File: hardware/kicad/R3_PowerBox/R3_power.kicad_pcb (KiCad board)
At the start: 2 copper layers, 160 x 80 mm, 0 parts

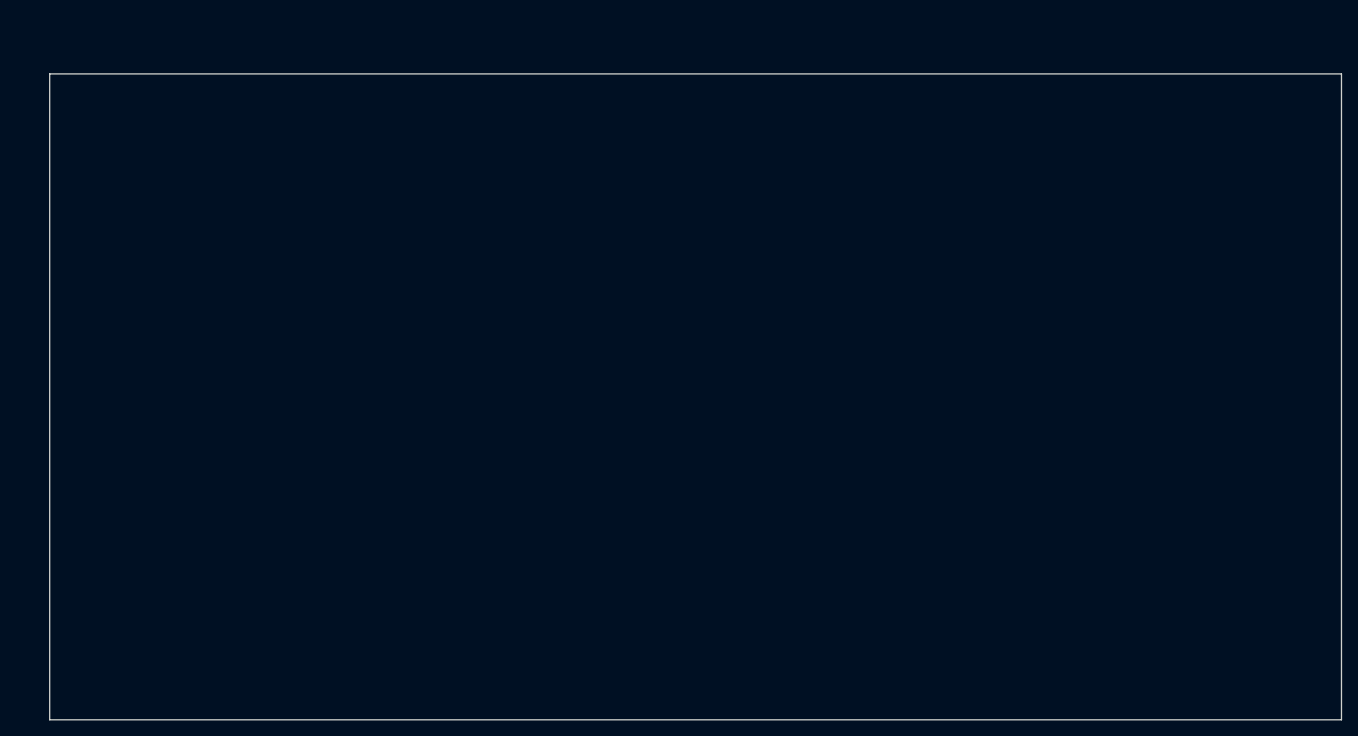
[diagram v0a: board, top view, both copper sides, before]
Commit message: Finalize R3 PowerBox pre-routing placement
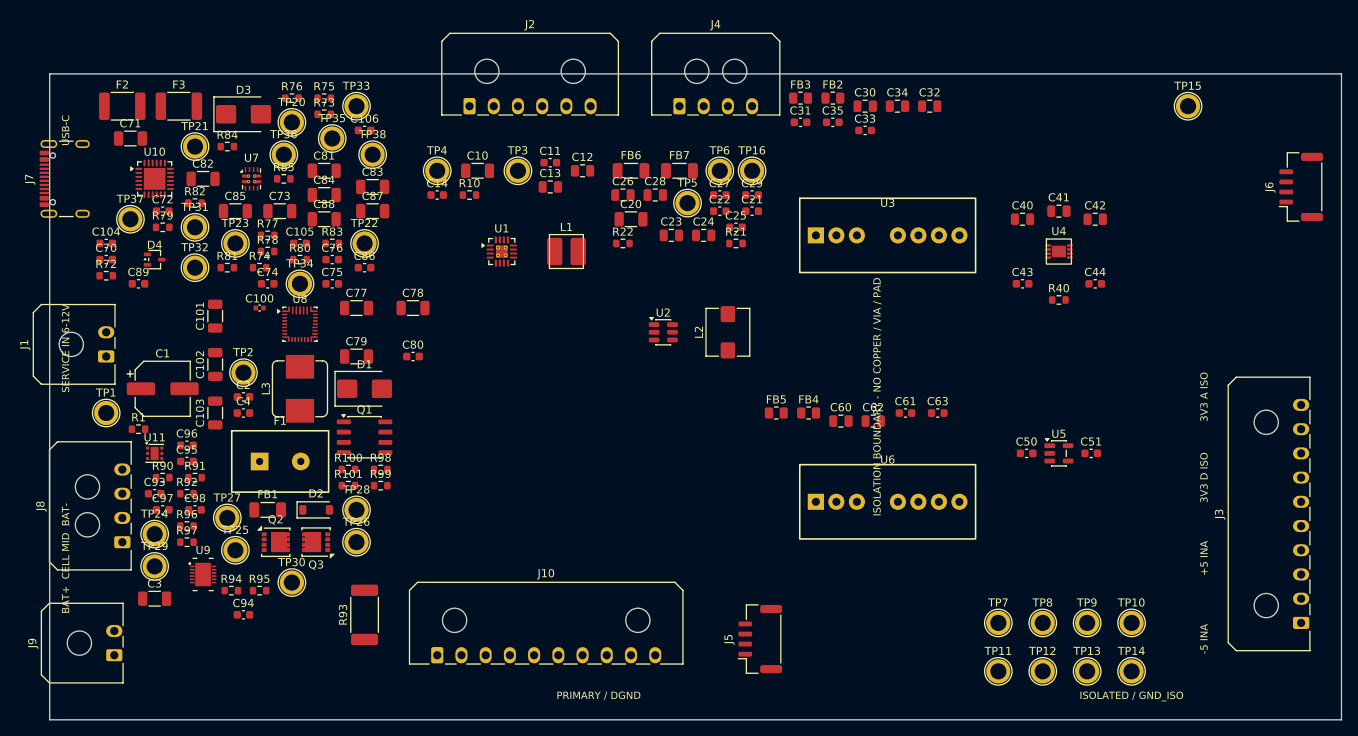
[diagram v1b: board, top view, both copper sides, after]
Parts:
- added C1: 47uF/25V low-ESR, CP_Elec_6.3x5.8, F.Cu at (34.0, 59.0)
- added C10: 10uF/25V, C_1206_3216Metric, F.Cu at (73.0, 32.0)
- added C100: 100nF/25V VBUS LOCAL, C_0402_1005Metric, F.Cu at (46.0, 49.0)
- added C101: 10uF/25V VBUS LOCAL, C_1206_3216Metric, F.Cu at (40.5, 50.0)
- added C102: 10uF/25V VBUS LOCAL, C_1206_3216Metric, F.Cu at (40.5, 56.0)
- added C103: 10uF/25V VBUS LOCAL, C_1206_3216Metric, F.Cu at (40.5, 62.0)
- added C104: 1uF VREG_1V2, C_0603_1608Metric, F.Cu at (27.0, 41.0)
- added C105: 1uF VREG_2V7, C_0603_1608Metric, F.Cu at (51.0, 41.0)
- added C106: 4.7uF/25V PD VDD, C_0603_1608Metric, F.Cu at (59.0, 27.0)
- added C11: 100nF/25V, C_0603_1608Metric, F.Cu at (82.0, 31.0)
- added C12: 22uF/10V, C_0805_2012Metric, F.Cu at (86.0, 32.0)
- added C13: 22uF/10V, C_0805_2012Metric, F.Cu at (82.0, 34.0)
- added C14: 3.3nF, C_0603_1608Metric, F.Cu at (68.0, 35.0)
- added C2: 100nF/25V, C_0603_1608Metric, F.Cu at (44.0, 60.0)
- added C20: 10uF/25V, C_1206_3216Metric, F.Cu at (92.0, 38.0)
- added C21: 100nF/25V, C_0603_1608Metric, F.Cu at (107.0, 37.0)
- added C22: 100nF BOOT, C_0603_1608Metric, F.Cu at (103.0, 37.0)
- added C23: 22uF/10V, C_0805_2012Metric, F.Cu at (97.0, 40.0)
- added C24: 22uF/10V, C_0805_2012Metric, F.Cu at (101.0, 40.0)
- added C25: 75pF C0G, C_0603_1608Metric, F.Cu at (105.0, 39.0)
- added C26: 10uF/10V ADS IN, C_0805_2012Metric, F.Cu at (91.0, 35.0)
- added C27: 100nF ADS IN, C_0603_1608Metric, F.Cu at (103.0, 35.0)
- added C28: 10uF/10V INA IN, C_0805_2012Metric, F.Cu at (95.0, 35.0)
- added C29: 100nF INA IN, C_0603_1608Metric, F.Cu at (107.0, 35.0)
- added C3: 22uF/25V, C_1206_3216Metric, F.Cu at (33.0, 85.0)
- added C30: 10uF/10V RAW, C_0805_2012Metric, F.Cu at (121.0, 24.0)
- added C31: 100nF RAW, C_0603_1608Metric, F.Cu at (113.0, 26.0)
- added C32: 10uF A bulk, C_0805_2012Metric, F.Cu at (129.0, 24.0)
- added C33: 100nF A, C_0603_1608Metric, F.Cu at (121.0, 27.0)
- added C34: 10uF D bulk, C_0805_2012Metric, F.Cu at (125.0, 24.0)
- added C35: 100nF D, C_0603_1608Metric, F.Cu at (117.0, 26.0)
- added C4: 100nF/25V, C_0603_1608Metric, F.Cu at (44.0, 62.0)
- added C40: 10uF VIN, C_0805_2012Metric, F.Cu at (140.5, 38.0)
- added C41: 10uF VREG, C_0805_2012Metric, F.Cu at (145.0, 37.0)
- added C42: 10uF VOUT, C_0805_2012Metric, F.Cu at (149.5, 38.0)
- added C43: 1uF REF, C_0603_1608Metric, F.Cu at (140.5, 46.0)
- added C44: 1uF BYP, C_0603_1608Metric, F.Cu at (149.5, 46.0)
- added C50: 2.2uF IN, C_0603_1608Metric, F.Cu at (141.0, 67.0)
- added C51: 4.7uF OUT, C_0603_1608Metric, F.Cu at (149.0, 67.0)
- added C60: 10uF +5V bulk, C_0805_2012Metric, F.Cu at (118.0, 63.0)
- added C61: 100nF +5V, C_0603_1608Metric, F.Cu at (126.0, 62.0)
- added C62: 10uF -5V bulk, C_0805_2012Metric, F.Cu at (122.0, 63.0)
- added C63: 100nF -5V, C_0603_1608Metric, F.Cu at (130.0, 62.0)
- added C70: 4.7nF SHIELD, C_0603_1608Metric, F.Cu at (27.0, 43.0)
- added C71: 10uF/25V USB, C_1206_3216Metric, F.Cu at (30.0, 28.0)
- added C72: 100nF MUX SS, C_0603_1608Metric, F.Cu at (34.0, 37.0)
- added C73: 10uF/25V MUX OUT, C_1206_3216Metric, F.Cu at (48.5, 37.0)
- added C74: 47nF BTST1, C_0603_1608Metric, F.Cu at (47.0, 46.0)
- added C75: 47nF BTST2, C_0603_1608Metric, F.Cu at (55.0, 46.0)
- added C76: 4.7uF REGN, C_0603_1608Metric, F.Cu at (55.0, 43.0)
- added C77: 10uF/25V PMID, C_1206_3216Metric, F.Cu at (58.0, 49.0)
- added C78: 10uF/25V PMID, C_1206_3216Metric, F.Cu at (65.0, 49.0)
- added C79: 10uF/25V PMID, C_1206_3216Metric, F.Cu at (58.0, 55.0)
- added C80: 100nF PMID, C_0603_1608Metric, F.Cu at (65.0, 55.0)
- added C81: 10uF/16V SYS, C_1206_3216Metric, F.Cu at (54.0, 32.0)
- added C82: 10uF/16V SYS, C_1206_3216Metric, F.Cu at (39.0, 33.0)
- added C83: 10uF/16V SYS, C_1206_3216Metric, F.Cu at (60.0, 34.0)
- added C84: 10uF/16V SYS, C_1206_3216Metric, F.Cu at (54.0, 35.0)
- added C85: 10uF/16V SYS, C_1206_3216Metric, F.Cu at (43.0, 37.0)
- added C86: 100nF SYS, C_0603_1608Metric, F.Cu at (59.0, 44.0)
- added C87: 10uF/16V BAT, C_1206_3216Metric, F.Cu at (60.0, 37.0)
- added C88: 10uF/16V BAT, C_1206_3216Metric, F.Cu at (54.0, 38.0)
- added C89: 1nF SDRV, C_0603_1608Metric, F.Cu at (31.0, 46.0)
- added C93: 2.2uF PBI, C_0603_1608Metric, F.Cu at (33.0, 72.0)
- added C94: 100nF SHUNT DIFF, C_0603_1608Metric, F.Cu at (44.0, 87.0)
- added C95: 100nF DSG D-S / TI EVM, C_0603_1608Metric, F.Cu at (37.0, 68.0)
- added C96: 100nF CHG D-S / TI EVM, C_0603_1608Metric, F.Cu at (37.0, 66.0)
- added C97: 100nF VC2-VC1 / CELL2, C_0603_1608Metric, F.Cu at (34.0, 74.0)
- added C98: 100nF VC1-VSS / CELL1, C_0603_1608Metric, F.Cu at (38.0, 74.0)
- added D1: SMBJ13A / 13V VRWM, D_SMB, F.Cu at (59.0, 59.0)
- added D2: BZT52C10, D_SOD-123, F.Cu at (53.0, 74.0)
- added D3: SMBJ13A / 13V VRWM USB VBUS, D_SMB, F.Cu at (44.0, 25.0)
- added D4: ESDA25W CC ESD / P1,P2=CC P3=GND, SOT-323_SC-70, F.Cu at (33.0, 43.0)
- added F1: MF-R250-0-10 2.5A/30V PPTC, Fuse_PTC_MF-R250, F.Cu at (46.0, 68.0)
- added F2: MF-MSMF260/16X-2 2.6A/16V PPTC, Fuse_1812_4532Metric_Pad1.30x3.40mm_HandSolder, F.Cu at (29.0, 24.0)
- added F3: MF-MSMF250/16X-2 2.5A/16V PPTC, Fuse_1812_4532Metric_Pad1.30x3.40mm_HandSolder, F.Cu at (36.0, 24.0)
- added FB1: BLM31PG601SN1, L_1206_3216Metric_Pad1.22x1.90mm_HandSolder, F.Cu at (47.0, 74.0)
- added FB2: FB_A / FB-or-0R, R_0805_2012Metric, F.Cu at (117.0, 23.0)
- added FB3: FB_D / FB-or-0R, R_0805_2012Metric, F.Cu at (113.0, 23.0)
- added FB4: FB_INA_P / FB-or-0R, R_0805_2012Metric, F.Cu at (114.0, 62.0)
- added FB5: FB_INA_N / FB-or-0R, R_0805_2012Metric, F.Cu at (110.0, 62.0)
- added FB6: BLM31KN601B family / 2A, L_1206_3216Metric_Pad1.22x1.90mm_HandSolder, F.Cu at (92.0, 32.0)
- added FB7: BLM31KN601B family / 2A, L_1206_3216Metric_Pad1.22x1.90mm_HandSolder, F.Cu at (98.0, 32.0)
- added J1: SERVICE / BENCH INPUT 6-12V, Molex_Micro-Fit_3.0_43650-0200_1x02_P3.00mm_Horizontal, F.Cu at (27.0, 55.0)
- added J10: BATTERY / CHARGER TELEMETRY, Molex_Micro-Fit_3.0_43650-1000_1x10_P3.00mm_Horizontal, F.Cu at (68.0, 92.0)
- added J2: DIGITAL POWER OUT, Molex_Micro-Fit_3.0_43650-0600_1x06_P3.00mm_Horizontal, F.Cu at (72.0, 24.0)
- added J3: ISOLATED POWER OUT, Molex_Micro-Fit_3.0_43650-1000_1x10_P3.00mm_Horizontal, F.Cu at (175.0, 88.0)
- added J4: CONTROL / SERVICE, Molex_Micro-Fit_3.0_43650-0400_1x04_P3.00mm_Horizontal, F.Cu at (98.0, 24.0)
- added J5: PRIMARY AUX DNP, JST_GH_SM04B-GHS-TB_1x04-1MP_P1.25mm_Horizontal, F.Cu at (108.0, 90.0)
- added J6: ISOLATED AUX DNP, JST_GH_SM04B-GHS-TB_1x04-1MP_P1.25mm_Horizontal, F.Cu at (175.0, 34.0)
- added J7: USB-C POWER INPUT, USB_C_Receptacle_GCT_USB4105-xx-A_16P_TopMnt_Horizontal, F.Cu at (23.0, 33.0)
- added J8: 2S BATTERY / KEYED / NTC_BMS=103AT-2, Molex_Micro-Fit_3.0_43650-0400_1x04_P3.00mm_Horizontal, F.Cu at (29.0, 78.0)
- added J9: NTC_CHG=103AT-2 / QUIET DGND RETURN, Molex_Micro-Fit_3.0_43650-0200_1x02_P3.00mm_Horizontal, F.Cu at (28.0, 92.0)
- added L1: 2.2uH XFL4020-222ME, L_Coilcraft_XFL4020, F.Cu at (84.0, 42.0)
- added L2: 10uH SRP5030TA-100M, L_Bourns_SRP5030T, F.Cu at (104.0, 52.0)
- added L3: 1.0uH >=6A / MPN TBD, L_Bourns_SRP7028A_7.3x6.6mm, F.Cu at (51.0, 59.0)
- added Q1: DMP3010LSS-13, SO-8_3.9x4.9mm_P1.27mm, F.Cu at (59.0, 65.0)
- added Q2: CSD17577Q3AT 30V NMOS DSG, CSD17577Q3A_VSON-8_3.3x3.3mm, F.Cu at (48.0, 78.0)
- added Q3: CSD17577Q3AT 30V NMOS CHG, CSD17577Q3A_VSON-8_3.3x3.3mm, F.Cu at (53.0, 78.0)
- added R1: 100k, R_0603_1608Metric, F.Cu at (31.0, 64.0)
- added R10: 100k, R_0603_1608Metric, F.Cu at (72.0, 35.0)
- added R100: 5.1k CHG GATE / TI EVM, R_0603_1608Metric, F.Cu at (57.0, 69.0)
- added R101: 10M CHG G-S / TI EVM, R_0603_1608Metric, F.Cu at (57.0, 71.0)
- added R21: 100k 1%, R_0603_1608Metric, F.Cu at (105.0, 41.0)
- added R22: 13.3k 1%, R_0603_1608Metric, F.Cu at (91.0, 41.0)
- added R40: 10k, R_0603_1608Metric, F.Cu at (145.0, 48.0)
- added R72: 1M SHIELD, R_0603_1608Metric, F.Cu at (27.0, 45.0)
- added R73: 44.2k / ILIM typ 2.5A, R_0603_1608Metric, F.Cu at (54.0, 25.0)
- added R74: 100R BATP, R_0603_1608Metric, F.Cu at (46.0, 44.0)
- added R75: 6.04k PROG / 2S PROFILE, R_0603_1608Metric, F.Cu at (54.0, 23.0)
- added R76: 243k ILIM TOP / DEFAULT 0.50A, R_0603_1608Metric, F.Cu at (50.0, 23.0)
- added R77: 100k ILIM BOT, R_0603_1608Metric, F.Cu at (47.0, 40.0)
- added R78: 5.24k TS TOP, R_0603_1608Metric, F.Cu at (47.0, 42.0)
- added R79: 30.31k TS BOT, R_0603_1608Metric, F.Cu at (34.0, 39.0)
- added R80: 10k STAT PU, R_0603_1608Metric, F.Cu at (51.0, 43.0)
- added R81: 10k INT PU, R_0603_1608Metric, F.Cu at (42.0, 44.0)
- added R82: 10k MUX ST PU, R_0603_1608Metric, F.Cu at (38.0, 36.0)
- added R83: 10k ALERT PU, R_0603_1608Metric, F.Cu at (55.0, 41.0)
- added R84: 10k PDO3 OK PU, R_0603_1608Metric, F.Cu at (42.0, 29.0)
- added R85: 0R PD VDD FEED, R_0603_1608Metric, F.Cu at (49.0, 33.0)
- added R90: 100R VC2 / KELVIN, R_0603_1608Metric, F.Cu at (34.0, 70.0)
- added R91: 100R VC1 / KELVIN, R_0603_1608Metric, F.Cu at (38.0, 70.0)
- added R92: 100R TS, R_0603_1608Metric, F.Cu at (37.0, 72.0)
- added R93: WSL2512R0100FEA 10mR 1W, R_2512_6332Metric_Pad1.40x3.35mm_HandSolder, F.Cu at (59.0, 87.0)
- added R94: 100R KELVIN, R_0603_1608Metric, F.Cu at (42.5, 84.0)
- added R95: 100R KELVIN, R_0603_1608Metric, F.Cu at (46.0, 84.0)
- added R96: 10k I2C, R_0603_1608Metric, F.Cu at (37.0, 76.0)
- added R97: 10k I2C, R_0603_1608Metric, F.Cu at (37.0, 78.0)
- added R98: 5.1k DSG GATE / TI EVM, R_0603_1608Metric, F.Cu at (61.0, 69.0)
- added R99: 10M DSG G-S / TI EVM, R_0603_1608Metric, F.Cu at (61.0, 71.0)
- added TP1: SERVICE_IN_RAW, TestPoint_Plated_Hole_D2.0mm, F.Cu at (27.0, 62.0)
- added TP10: GND_ISO, TestPoint_Plated_Hole_D2.0mm, F.Cu at (154.0, 88.0)
- added TP11: +3V3_A_ISO, TestPoint_Plated_Hole_D2.0mm, F.Cu at (137.5, 94.0)
- added TP12: +3V3_D_ISO, TestPoint_Plated_Hole_D2.0mm, F.Cu at (143.0, 94.0)
- added TP13: +5V_INA, TestPoint_Plated_Hole_D2.0mm, F.Cu at (148.5, 94.0)
- added TP14: -5V_INA, TestPoint_Plated_Hole_D2.0mm, F.Cu at (154.0, 94.0)
- added TP15: DGND, TestPoint_Plated_Hole_D2.0mm, F.Cu at (161.0, 24.0)
- added TP16: +5V_PREISO_INA, TestPoint_Plated_Hole_D2.0mm, F.Cu at (107.0, 32.0)
- added TP2: SERVICE_IN_PROT, TestPoint_Plated_Hole_D2.0mm, F.Cu at (44.0, 57.0)
- added TP20: USB_VBUS_RAW, TestPoint_Plated_Hole_D2.0mm, F.Cu at (50.0, 26.0)
- added TP21: CHARGER_IN, TestPoint_Plated_Hole_D2.0mm, F.Cu at (38.0, 29.0)
- added TP22: VSYS_RAW, TestPoint_Plated_Hole_D2.0mm, F.Cu at (59.0, 41.0)
- added TP23: VSYS_PROT, TestPoint_Plated_Hole_D2.0mm, F.Cu at (43.0, 41.0)
- added TP24: BAT_POS_RAW, TestPoint_Plated_Hole_D2.0mm, F.Cu at (33.0, 77.0)
- added TP25: CELL_MID, TestPoint_Plated_Hole_D2.0mm, F.Cu at (43.0, 79.0)
- added TP26: BAT_NEG_RAW, TestPoint_Plated_Hole_D2.0mm, F.Cu at (58.0, 78.0)
- added TP27: BMS_SRP_FILT, TestPoint_Plated_Hole_D2.0mm, F.Cu at (42.0, 75.0)
- added TP28: BMS_SRN_FILT, TestPoint_Plated_Hole_D2.0mm, F.Cu at (58.0, 74.0)
- added TP29: NTC_BMS, TestPoint_Plated_Hole_D2.0mm, F.Cu at (33.0, 81.0)
- added TP3: +3V3_D, TestPoint_Plated_Hole_D2.0mm, F.Cu at (78.0, 32.0)
- added TP30: NTC_CHG, TestPoint_Plated_Hole_D2.0mm, F.Cu at (50.0, 83.0)
- added TP31: USB_CC1, TestPoint_Plated_Hole_D2.0mm, F.Cu at (38.0, 39.0)
- added TP32: USB_CC2, TestPoint_Plated_Hole_D2.0mm, F.Cu at (38.0, 44.0)
- added TP33: USB_VBUS_PROT, TestPoint_Plated_Hole_D2.0mm, F.Cu at (58.0, 24.0)
- added TP34: PD_VDD, TestPoint_Plated_Hole_D2.0mm, F.Cu at (51.0, 46.0)
- added TP35: PD_VREG_2V7, TestPoint_Plated_Hole_D2.0mm, F.Cu at (55.0, 28.0)
- added TP36: PD_ALERT_N, TestPoint_Plated_Hole_D2.0mm, F.Cu at (49.0, 30.0)
- added TP37: PM_I2C_SCL, TestPoint_Plated_Hole_D2.0mm, F.Cu at (30.0, 38.0)
- added TP38: PM_I2C_SDA, TestPoint_Plated_Hole_D2.0mm, F.Cu at (60.0, 30.0)
- added TP4: PG_3V3_D, TestPoint_Plated_Hole_D2.0mm, F.Cu at (68.0, 32.0)
- added TP5: +5V_PREISO, TestPoint_Plated_Hole_D2.0mm, F.Cu at (99.0, 36.0)
- added TP6: +5V_PREISO_ADS, TestPoint_Plated_Hole_D2.0mm, F.Cu at (103.0, 32.0)
- added TP7: +5V_ISO_RAW, TestPoint_Plated_Hole_D2.0mm, F.Cu at (137.5, 88.0)
- added TP8: +5V_ISO_A, TestPoint_Plated_Hole_D2.0mm, F.Cu at (143.0, 88.0)
- added TP9: +5V_ISO_D, TestPoint_Plated_Hole_D2.0mm, F.Cu at (148.5, 88.0)
- added U1: TPS62132RGTR, VQFN-16-1EP_3x3mm_P0.5mm_EP1.45x1.45mm_ThermalVias, F.Cu at (76.0, 42.0)
- added U10: STUSB4500QTR, QFN-24-1EP_4x4mm_P0.5mm_EP2.7x2.7mm, F.Cu at (33.0, 33.0)
- added U11: BQ294502 SPACE ONLY / NC / DNP, WSON-6-1EP_2x2mm_P0.65mm_EP1x1.6mm, F.Cu at (33.0, 67.0)
- added U2: TPS54302DDCR, SOT-23-6, F.Cu at (96.0, 52.0)
- added U3: RS3E-0505S/H3, Converter_DCDC_RECOM_RS3E_SIP8, F.Cu at (114.9, 40.0)
- added U4: ADM7150ACPZ-3.3-R7, LFCSP-8-1EP_3x3mm_P0.5mm_EP1.74x1.45mm, F.Cu at (145.0, 42.0)
- added U5: TPS7A2033PDBVR, SOT-23-5, F.Cu at (145.0, 67.0)
- added U6: RS3-0505D/H3, Converter_DCDC_RECOM_RS3_SIP8, F.Cu at (114.9, 73.0)
- added U7: TPS2121RUXR, Texas_VQFN-HR-12_2x2.5mm_P0.5mm_ThermalVias, F.Cu at (45.0, 33.0)
- added U8: BQ25798RQM, Texas_RQM0029A_VQFN-29_4x4mm_P0.4mm, F.Cu at (51.0, 51.0)
- added U9: BQ28Z610DRZR, Texas_DRZ0012A_VSON-12, F.Cu at (39.0, 82.0)
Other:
- copper layers 2 -> 4
- board text added: "+5 INA"
- board text added: "-5 INA"
- board text added: "3V3 A ISO"
- board text added: "3V3 D ISO"
- board text added: "BAT+ CELL MID BAT-"
- board text added: "ISOLATED / GND_ISO"
- board text added: "ISOLATION BOUNDARY - NO COPPER / VIA / PAD"
- board text added: "PRIMARY / DGND"
- board text added: "SERVICE IN 6-12V"
- board text added: "THERMAL COPPER + VIAS: BQ25798"
- board text added: "THERMAL COPPER + VIAS: Q2/Q3"
- board text added: "THERMAL COPPER + VIAS: TPS2121"
- board text added: "THERMAL COPPER + VIAS: TPS54302"
- board text added: "THERMAL COPPER + VIAS: TPS62132"
- board text added: "THERMAL COPPER IF LOSS REQUIRES: ADM7150"
- board text added: "THERMAL COPPER: SHUNT"
- board text added: "USB-C"

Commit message: Finalize R3 PowerBox user power controls
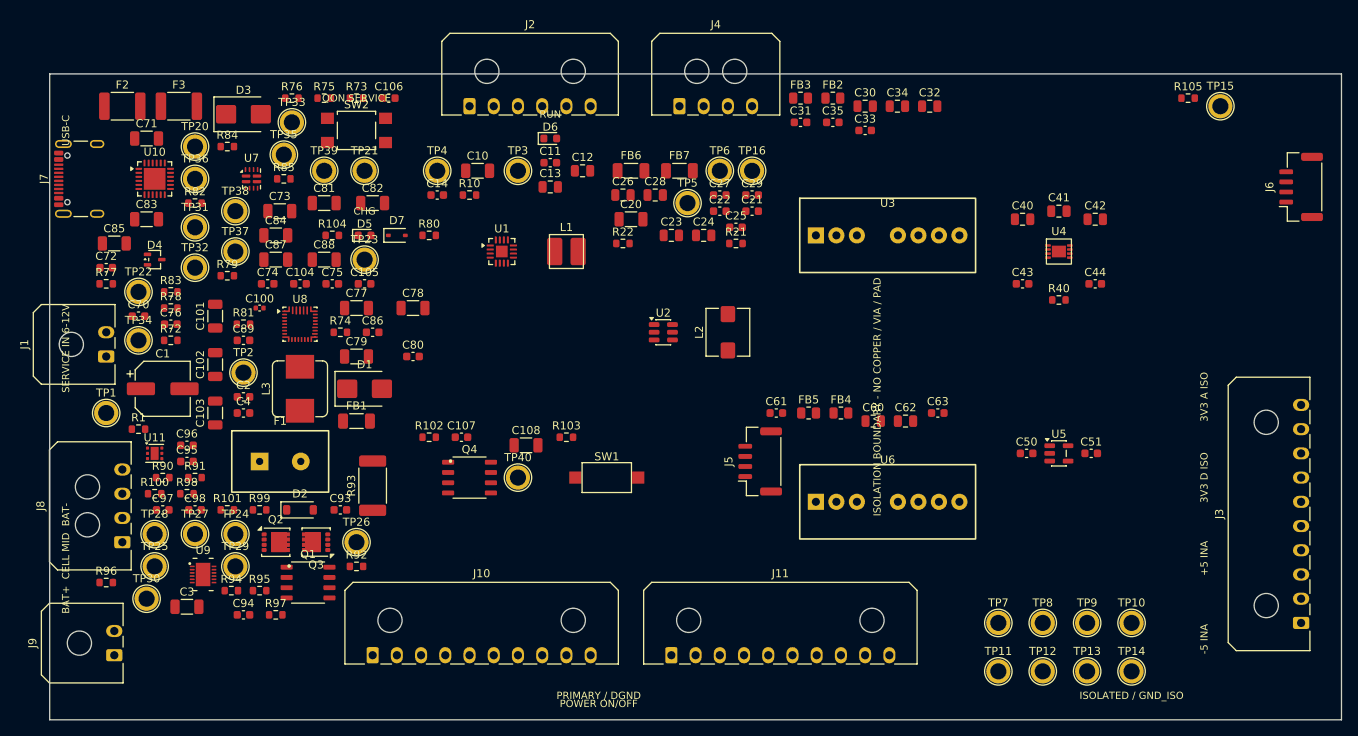
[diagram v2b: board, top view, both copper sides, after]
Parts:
- added C107: 100nF G-S / SOFT START, C_0603_1608Metric, F.Cu at (71.0, 65.0)
- added C108: 10uF/16V VSYS_MAIN, C_1206_3216Metric, F.Cu at (79.0, 66.0)
- added D5: LTST-C190KRKT RED / CHG, LED_0603_1608Metric, F.Cu at (59.0, 40.0)
- added D6: LTST-C190KGKT GREEN / RUN, LED_0603_1608Metric, F.Cu at (82.0, 28.0)
- added D7: BAT54WS-7-F STAT ISOLATION, D_SOD-323, F.Cu at (63.0, 40.0)
- added J11: USER PANEL / PRIMARY ONLY, Molex_Micro-Fit_3.0_43650-1000_1x10_P3.00mm_Horizontal, F.Cu at (97.0, 92.0)
- added Q4: DMP3007LSS-13 SYSTEM LOAD SWITCH, DMP3007LSS_SO8_LOGICAL, F.Cu at (72.0, 70.0)
- added R102: 100k G-S / DEFAULT OFF, R_0603_1608Metric, F.Cu at (67.0, 65.0)
- added R103: 10k GATE SERIES, R_0603_1608Metric, F.Cu at (84.0, 65.0)
- added R104: 2.2k CHG LED / ~1.3mA, R_0603_1608Metric, F.Cu at (55.0, 40.0)
- added R105: 2.2k RUN LED / ~0.7mA, R_0603_1608Metric, F.Cu at (161.0, 23.0)
- added SW1: C&K RS282G05A3 / POWER ON, SW_SPST_CK_RS282G05A3, F.Cu at (89.0, 70.0)
- added SW2: QON SERVICE / TL3305AF160QG, SW_SPST_TL3305A, F.Cu at (58.0, 27.0)
- added TP39: QON_SERVICE, TestPoint_Plated_Hole_D2.0mm, F.Cu at (54.0, 32.0)
- added TP40: VSYS_MAIN, TestPoint_Plated_Hole_D2.0mm, F.Cu at (78.0, 70.0)
- Q1: value DMP3010LSS-13 -> DMP3007LSS-13; footprint SO-8_3.9x4.9mm_P1.27mm -> DMP3007LSS_SO8_LOGICAL
- R80: value 10k STAT PU -> 10k CHARGE_STATUS PU
- U1: footprint VQFN-16-1EP_3x3mm_P0.5mm_EP1.45x1.45mm_ThermalVias -> VQFN-16-1EP_3x3mm_P0.5mm_EP1.45x1.45mm
- U7: footprint Texas_VQFN-HR-12_2x2.5mm_P0.5mm_ThermalVias -> Texas_VQFN-HR-12_2x2.5mm_P0.5mm
- moved TP22 28.6 mm to (31.0, 47.0)
- moved C83 28.3 mm to (32.0, 38.0)
- moved TP28 25.2 mm to (33.0, 77.0)
- moved C104 24.5 mm to (51.0, 46.0)
- moved R100 24.2 mm to (33.0, 72.0)
- moved R98 24.2 mm to (37.0, 72.0)
- moved C93 23.1 mm to (56.0, 74.0)
- moved R92 22.8 mm to (58.0, 81.0)
- moved J5 22.0 mm to (108.0, 68.0)
- moved C76 21.5 mm to (35.0, 51.0)
- moved C82 21.2 mm to (60.0, 36.0)
- moved TP21 21.2 mm to (59.0, 32.0)
- moved TP34 21.2 mm to (31.0, 53.0)
- moved R77 20.9 mm to (27.0, 46.0)
- moved R83 20.9 mm to (35.0, 47.0)
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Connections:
- C10 pad 1: VSYS_PROT -> VSYS_MAIN
- C11 pad 1: VSYS_PROT -> VSYS_MAIN
- C20 pad 1: VSYS_PROT -> VSYS_MAIN
- C21 pad 1: VSYS_PROT -> VSYS_MAIN
- U1 pad 10: VSYS_PROT -> VSYS_MAIN
- U1 pad 11: VSYS_PROT -> VSYS_MAIN
- U1 pad 12: VSYS_PROT -> VSYS_MAIN
- U1 pad 13: VSYS_PROT -> VSYS_MAIN
- U2 pad 3: VSYS_PROT -> VSYS_MAIN
- U2 pad 5: VSYS_PROT -> VSYS_MAIN
- U8 pad 1: CHARGE_STATUS -> BQ_STAT_RAW
- U8 pad 12: unconnected-(U8-QON-Pad12) -> QON_SERVICE
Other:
- board text added: "CHG"
- board text added: "POWER ON/OFF"
- board text added: "QON SERVICE"
- board text added: "RUN"

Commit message: Finalize R3 PowerBox mechanical interconnect
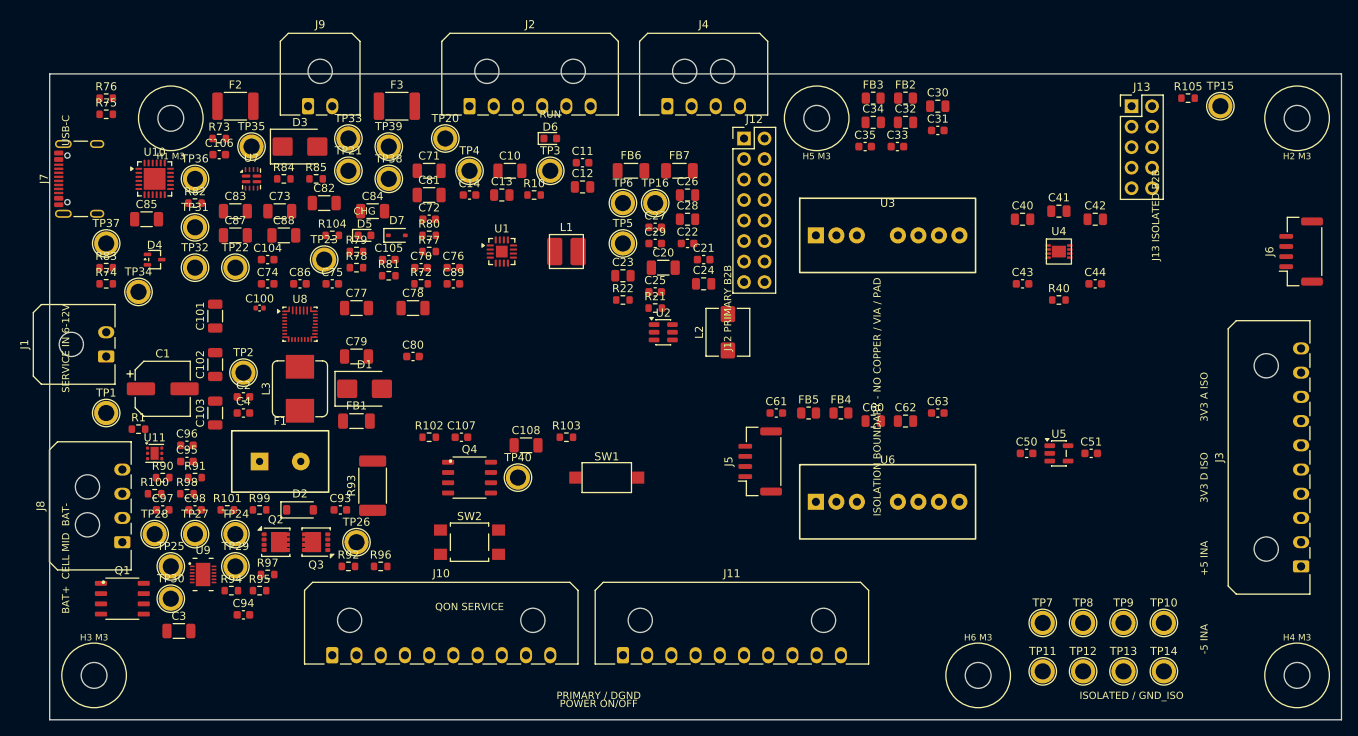
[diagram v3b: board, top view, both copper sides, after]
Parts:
- added H1: M3 NPTH 3.2mm / 8mm KEEPOUT, MountingHole_M3_NPTH_3.2mm_Keepout8mm, F.Cu at (35.0, 25.5)
- added H2: M3 NPTH 3.2mm / 8mm KEEPOUT, MountingHole_M3_NPTH_3.2mm_Keepout8mm, F.Cu at (174.5, 25.5)
- added H3: M3 NPTH 3.2mm / 8mm KEEPOUT, MountingHole_M3_NPTH_3.2mm_Keepout8mm, F.Cu at (25.5, 94.5)
- added H4: M3 NPTH 3.2mm / 8mm KEEPOUT, MountingHole_M3_NPTH_3.2mm_Keepout8mm, F.Cu at (174.5, 94.5)
- added H5: M3 NPTH 3.2mm / 8mm KEEPOUT, MountingHole_M3_NPTH_3.2mm_Keepout8mm, F.Cu at (115.0, 25.5)
- added H6: M3 NPTH 3.2mm / 8mm KEEPOUT, MountingHole_M3_NPTH_3.2mm_Keepout8mm, F.Cu at (135.0, 94.5)
- added J12: PRIMARY B2B 2x8 / DNP, PinHeader_2x08_P2.54mm_Vertical, F.Cu at (106.0, 28.0)
- added J13: ISOLATED B2B 2x5 / DNP, PinHeader_2x05_P2.54mm_Vertical, F.Cu at (154.0, 24.0)
- moved J9 72.1 mm to (52.0, 24.0), turned to 0 degrees
- moved SW2 52.9 mm to (72.0, 78.0)
- moved C72 40.4 mm to (67.0, 38.0)
- moved R77 40.2 mm to (67.0, 42.0)
- moved C76 35.7 mm to (70.0, 44.0)
- moved C70 35.5 mm to (66.0, 44.0)
- moved C71 35.2 mm to (67.0, 32.0)
- moved R96 34.1 mm to (61.0, 81.0)
- moved R72 31.8 mm to (66.0, 46.0)
- moved TP20 31.0 mm to (69.0, 28.0)
- moved R74 29.6 mm to (27.0, 46.0)
- moved R75 27.1 mm to (27.0, 25.0)
- moved F3 27.0 mm to (63.0, 24.0)
- moved C89 26.9 mm to (70.0, 46.0)
- moved R78 23.5 mm to (58.0, 44.0)
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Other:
- board text added: "FUTURE R3 UPPER BOARD REFERENCE / NOT EDGE.CUTS"
- board text added: "H1 M3"
- board text added: "H2 M3"
- board text added: "H3 M3"
- board text added: "H4 M3"
- board text added: "H5 M3"
- board text added: "H6 M3"
- board text added: "J12 PRIMARY B2B"
- board text added: "J13 ISOLATED B2B"

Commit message: Checkpoint R3 routing A0: repair isolation placement and start power loops
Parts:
- C74, C75: moved to B.Cu
- moved R105 76.2 mm to (85.0, 28.0)
- moved TP15 64.4 mm to (111.0, 59.0)
- moved C85 38.4 mm to (70.0, 43.5), turned to 90 degrees
- moved FB3 31.6 mm to (128.0, 54.0)
- moved C61 30.5 mm to (133.0, 82.0)
- moved C35 30.5 mm to (133.0, 57.0)
- moved C34 30.1 mm to (133.0, 54.0)
- moved TP22 28.2 mm to (69.0, 55.0)
- moved FB5 27.8 mm to (128.0, 86.0)
- moved C105 27.2 mm to (35.0, 40.0), turned to 90 degrees
- moved C63 27.1 mm to (128.0, 89.0)
- moved C76 25.2 mm to (46.5, 53.0), turned to 90 degrees
- moved C78 24.6 mm to (41.0, 43.5), turned to 90 degrees
- moved TP23 24.1 mm to (72.0, 59.0)
- moved C62 24.0 mm to (133.0, 86.0)
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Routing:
- net PACK_POS: track 0.00 -> 59.1 mm, vias 0 -> 6
- net BAT_POS_RAW: track 0.00 -> 51.0 mm, vias 0 -> 3
- net DGND: track 0.00 -> 41.0 mm, vias 0 -> 32
- net VSYS_RAW: track 0.00 -> 27.3 mm
- net CHG_SW1: track 0.00 -> 19.9 mm, vias 0 -> 4
- net CHG_SW2: track 0.00 -> 19.1 mm, vias 0 -> 4
- net CHG_PMID: track 0.00 -> 18.9 mm
- net CHARGER_IN: track 0.00 -> 15.6 mm
- net CHG_REGN: track 0.00 -> 5.14 mm
- net N$7: track 0.00 -> 5.07 mm, vias 0 -> 1
- net BMS_FET_COMMON: track 0.00 -> 4.23 mm, vias 0 -> 3
- net N$8: track 0.00 -> 3.66 mm, vias 0 -> 1

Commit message: Route checkpoint A battery sense and charger local networks
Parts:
- C89, C93, C95, C96, C97, C98, R101, R74, R75, R76, R77, R78, R79, R90, R91, R92, R96, R97: moved to B.Cu
- moved TP30 60.0 mm to (90.0, 61.0)
- moved R76 50.9 mm to (62.0, 60.0), turned to 180 degrees
- moved R90 41.8 mm to (74.0, 82.0), turned to 180 degrees
- moved R91 41.8 mm to (78.0, 82.0), turned to 180 degrees
- moved C97 36.5 mm to (70.5, 74.5)
- moved C98 35.5 mm to (73.5, 74.5)
- moved R75 34.4 mm to (53.0, 47.5), turned to 180 degrees
- moved R74 29.6 mm to (55.0, 55.5), turned to 180 degrees
- moved R100 27.0 mm to (58.5, 81.0)
- moved U9 27.0 mm to (65.5, 76.9)
- moved R95 23.7 mm to (63.5, 68.0)
- moved R94 23.2 mm to (63.5, 74.0)
- moved C94 20.4 mm to (62.0, 77.5), turned to 90 degrees
- moved R101 18.9 mm to (58.0, 84.0), turned to -90 degrees
- moved R97 18.1 mm to (65.0, 84.0)
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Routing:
- net BAT_POS_RAW: track 51.0 -> 168.7 mm, vias 3 -> 5
- net BAT_NEG_RAW: track 0.00 -> 102.6 mm, vias 0 -> 6
- net CELL_MID: track 0.00 -> 96.2 mm, vias 0 -> 1
- net PACK_POS: track 59.1 -> 115.7 mm, vias 6 -> 10
- net NTC_BMS: track 0.00 -> 50.8 mm, vias 0 -> 2
- net NTC_CHG: track 0.00 -> 35.6 mm, vias 0 -> 2
- net CHG_REGN: track 5.14 -> 30.6 mm, vias 0 -> 2
- net N$2: track 0.00 -> 24.7 mm, vias 0 -> 2
- net N$3: track 0.00 -> 23.6 mm, vias 0 -> 2
- net DGND: track 41.0 -> 60.4 mm, vias 32 -> 40
- net BMS_VC1_FILT: track 0.00 -> 19.3 mm, vias 0 -> 1
- net BMS_SRN_FILT: track 0.00 -> 18.7 mm, vias 0 -> 2
- net BMS_VC2_FILT: track 0.00 -> 17.2 mm, vias 0 -> 1
- net BQ25798_ILIM: track 0.00 -> 17.1 mm, vias 0 -> 2
- net BMS_SRP_FILT: track 0.00 -> 15.6 mm, vias 0 -> 2
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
